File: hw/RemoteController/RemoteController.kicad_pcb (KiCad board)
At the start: 4 copper layers, 100 x 75 mm, 138 parts, among them J1 Conn_01x04_Pin, J2 Conn_01x04_Pin, J4 BWSMA-KWE-Z3.5*4.2, SW2 ST-0-102-A01-T000-LF, SW6 TS-1088-AR02016, SW7 TS-1088-AR02016, SW8 TS-1088-AR02016, SW9 TS-1088-AR02016, U1 LM358, U10 H3-TCD-12-222X+, U11 LM358, U13 nRF52810-QFxx, U14 LM358, U15 LM358, U16 H3-TCD-12-222X+, U17 AD8313xRM, U18 LM358, U2 TPS562200, U3 SPF5043Z, U4 MICRF220AYQS, U5 XA17-G4K, U6 MAX7044AKA, U8 AD8313xRM, U9 GVA-63, Y1 32 MHz, Y2 L327S13CU11L, Y4 13.56 MHz, Y5 32.768 KHz

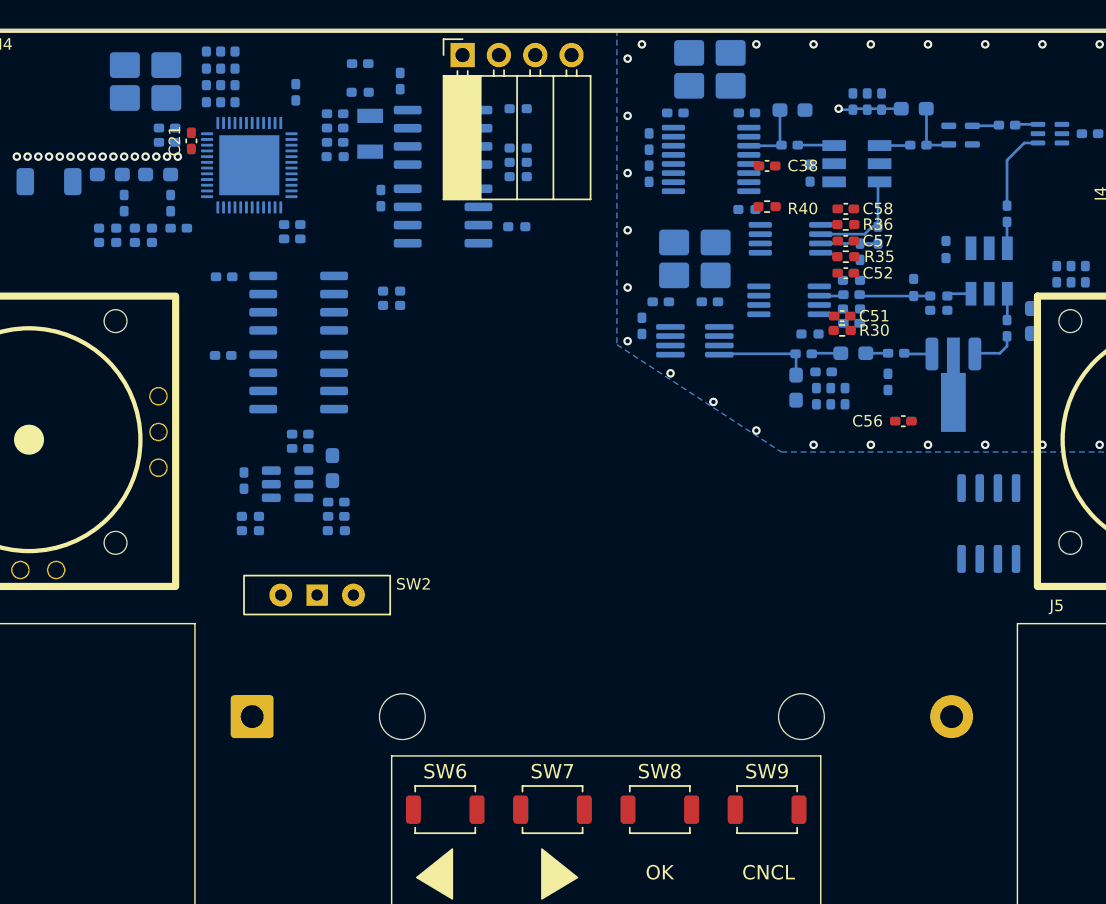
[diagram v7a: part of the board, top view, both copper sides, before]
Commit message: remote_ctrl: align everything pre-route
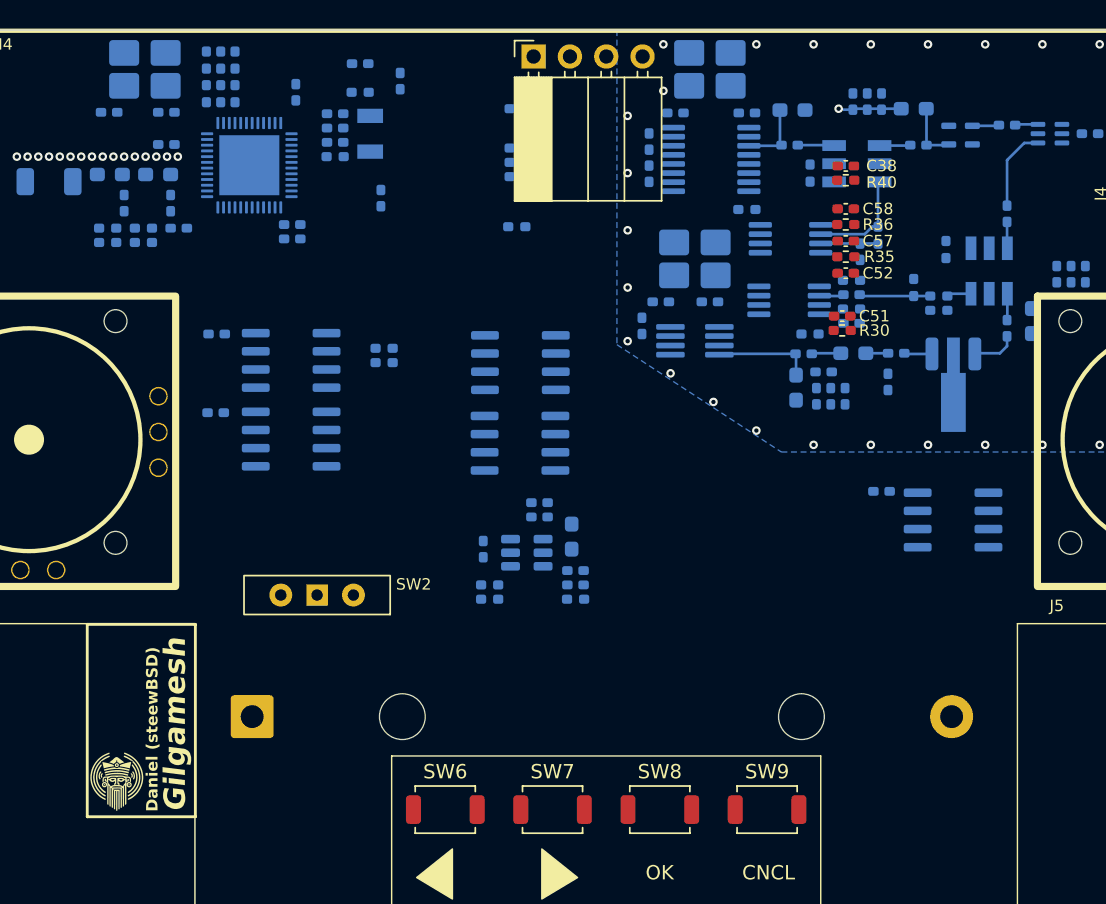
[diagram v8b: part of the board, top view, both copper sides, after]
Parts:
- C21, C56: moved to B.Cu
- moved C12 17.4 mm to (140.8, 92.0)
- moved C13 17.4 mm to (140.8, 91.0)
- moved L1 17.4 mm to (143.1, 93.4)
- moved C10 17.4 mm to (143.4, 96.8)
- moved C14 17.4 mm to (136.9, 94.3)
- moved C9 17.4 mm to (143.4, 95.8)
- moved R1 17.4 mm to (143.4, 97.8)
- moved R2 17.4 mm to (137.4, 96.8)
- moved R3 17.4 mm to (137.4, 97.8)
- moved U2 17.4 mm to (139.9, 94.5)
- moved U1 16.8 mm to (139.5, 86.9)
- moved U11 16.7 mm to (139.5, 81.2)
- moved R40 5.80 mm to (162.2, 68.5)
- moved C38 5.50 mm to (162.2, 67.5)
- moved C56 5.14 mm to (164.8, 90.2)
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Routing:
- net Net-(U13-DEC3): vias 0 -> 1
- net GND: vias 50 -> 49
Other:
- board text added: "Daniel (steewBSD)"
- board text added: "Gilgamesh"
